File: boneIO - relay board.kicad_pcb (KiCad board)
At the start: 2 copper layers, 197 x 102 mm, 92 parts, among them J1 Screw_Terminal_01x04, J10 Screw_Terminal_01x04, J11 Screw_Terminal_01x04, J12 Screw_Terminal_01x04, J13 Screw_Terminal_01x04, J2 Screw_Terminal_01x04, J3 Conn_02x04_Odd_Even, J4 Screw_Terminal_01x04, J5 Screw_Terminal_01x04, J6 Screw_Terminal_01x04, J7 Screw_Terminal_01x04, J8 Screw_Terminal_01x04, J9 Screw_Terminal_01x04, K1 RM85-2011-35-1024, K10 RM85-2011-35-1024, K11 RM85-2011-35-1024, K12 RM85-2011-35-1024, K13 RM85-2011-35-1024, K14 RM85-2011-35-1024, K15 RM85-2011-35-1024, K16 RM85-2011-35-1024, K17 RM85-2011-35-1024, K18 RM85-2011-35-1024, K19 RM85-2011-35-1024, K2 RM85-2011-35-1024, K20 RM85-2011-35-1024, K21 RM85-2011-35-1024, K22 RM85-2011-35-1024, K23 RM85-2011-35-1024, K24 RM85-2011-35-1024, K3 RM85-2011-35-1024, K4 RM85-2011-35-1024, K5 RM85-2011-35-1024, K6 RM85-2011-35-1024, K7 RM85-2011-35-1024, K8 RM85-2011-35-1024, K9 RM85-2011-35-1024, SW1 SW_DIP_x03, SW2 SW_DIP_x03, SW3 SW_DIP_x03, U1 MCP9808-E_SO8, U2 MCP9808-E_MS, U3 ULN2803A, U4 ULN2803A, U5 ULN2803A, U6 MCP23017_SS, U7 MCP23017_SS

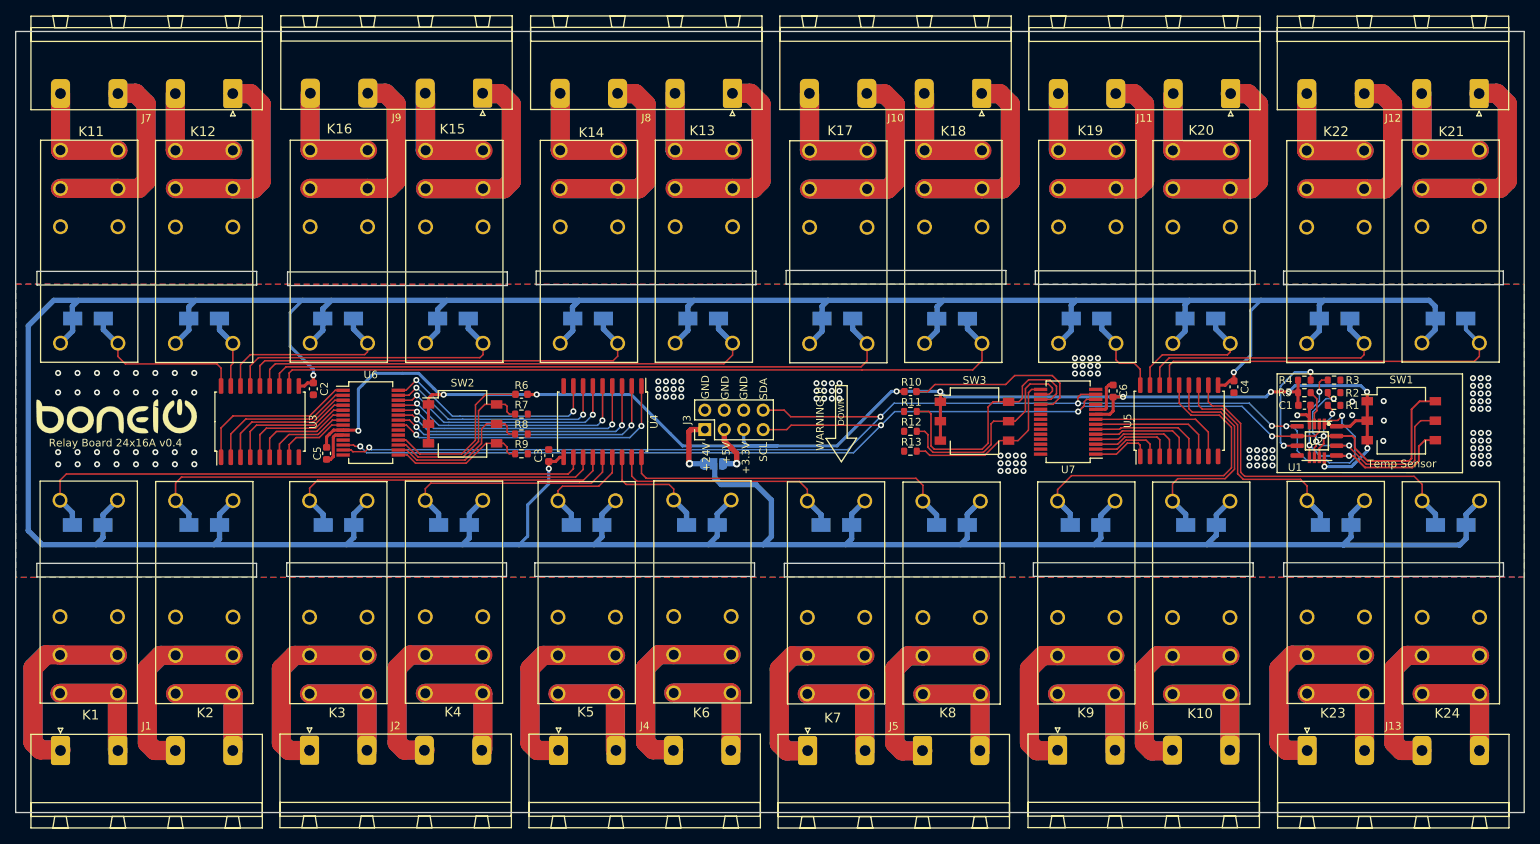
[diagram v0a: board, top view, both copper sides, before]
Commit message: relay board 24x16A v0.4 (rev2)
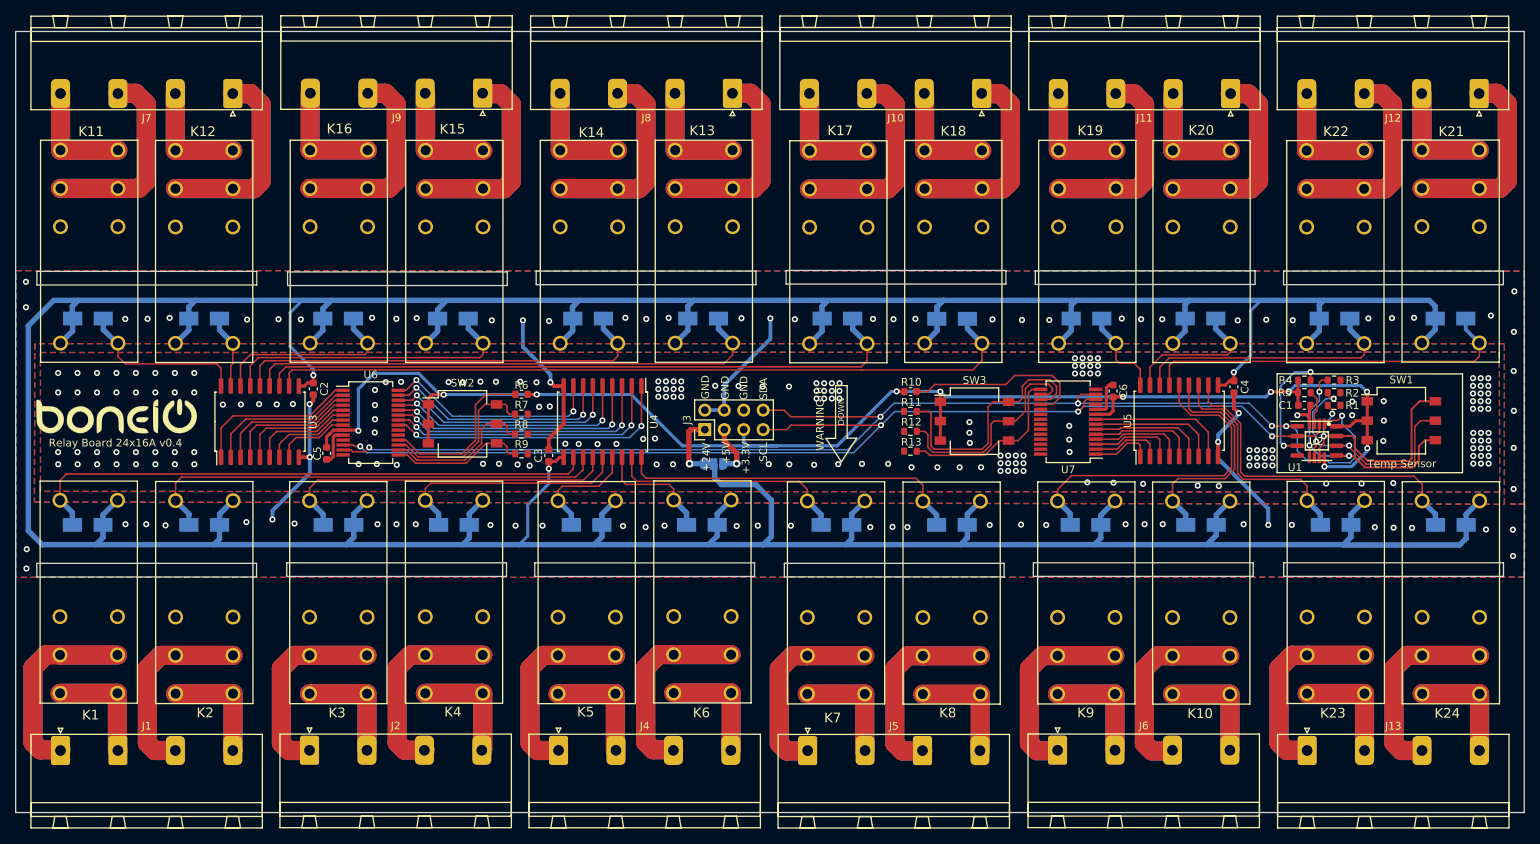
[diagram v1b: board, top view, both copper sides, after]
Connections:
- C2 pad 2: GND -> GND1
- C3 pad 2: GND -> GND1
- C4 pad 2: GND -> GND1
- J3 pad 2: GND -> GND1
- J3 pad 4: GND -> GND1
- U3 pad 9: GND -> GND1
- U4 pad 9: GND -> GND1
- U5 pad 9: GND -> GND1
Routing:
- net GND1: track 0.00 -> 80.8 mm, vias 0 -> 85
- net GND: vias 128 -> 190
- added copper zone on B.Cu, net GND1
- added copper zone on F.Cu, net GND1
